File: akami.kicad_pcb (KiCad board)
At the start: 4 copper layers, 30 x 33.3 mm, 55 parts, among them J1 USB_C_Receptacle_USB2.0, Q1 P MOSFET, Q2 P MOSFET, U1 nRF52840, U2 TP4054, U3 AP2112K-3.3, U4 ProMicro_2, Y1 32MHz, Y2 32.768 kHz

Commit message: more stuff
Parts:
- added J2: Conn_01x01, footprints:1pin_conn, F.Cu at (7.62, -15.2)
- added J3: Conn_01x01, footprints:1pin_conn, F.Cu at (-7.62, -15.2)
- added TP3: TestPoint, TestPoint:TestPoint_Pad_1.0x1.0mm, B.Cu at (0.00, -5.85)
- added TP4: TestPoint, footprints:circular-pad-0.3mm, F.Cu at (-5.15, 12.8)
- C17, C18: value 12pF -> 3.3pF
- C6, C7: value 12pF -> 10pF
- mouse-bite-2mm-slot (x2): footprint panelisation:mouse-bite-2mm-slot -> footprints:mouse-bite-2mm-slot-one-sided
- moved R2 7.52 mm to (-0.95, -1.62), turned to 0 degrees
- moved C13 2.00 mm to (-4.30, 0.55), turned to 270 degrees
- moved C2 0.28 mm to (-2.03, 0.55)
- moved R4 0.09 mm to (-0.65, -0.01)
- moved R7 0.05 mm to (3.70, -2.44)
- turned mouse-bite-2mm-slot to 270 degrees
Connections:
- net Net-(C22-Pad2) renamed ANTENNA
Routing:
- net USB_D-: track 23.3 -> 21.2 mm
- net VBUS: track 37.1 -> 35.2 mm, vias 5 -> 6
- net P0.08: track 19.6 -> 17.8 mm
- net POWER_CTRL: track 21.3 -> 23.1 mm
- net P0.06: track 21.0 -> 19.3 mm
- net VBAT: track 33.5 -> 35.1 mm, vias 4 -> 6
- net RESET: track 20.6 -> 19.4 mm
- net P0.11: track 15.3 -> 14.1 mm
- net Net-(C13-Pad1): track 3.64 -> 4.70 mm
- net VDD_NRF: track 11.7 -> 12.7 mm, vias 8 -> 9
- net Net-(L3-Pad2): track 10.5 -> 9.63 mm
- net GND: track 36.1 -> 35.3 mm, vias 31 -> 38
- net BAT_VOLT: track 12.4 -> 11.6 mm
- net Net-(C15-Pad2): track 22.0 -> 21.5 mm
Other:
- board text added: "VDD"

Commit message: stuff
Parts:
- added G***: LOGO, footprints:akami-logo, F.Cu at (0.00, 13.5)
- added G***: LOGO, footprints:akami-logo, B.Cu at (0.00, 14.5)
- added NT1: Net-Tie_2, footprints:net-tie-2-tiny, F.Cu at (1.50, 7.33)
- C12: value 820pF -> 1nF
- C17, C18: value 3.3pF -> 15pF
- Q1, Q2: value P MOSFET -> AO3401A
- Y2: footprint Crystal:Crystal_SMD_2012-2Pin_2.0x1.2mm -> Crystal:Crystal_SMD_3215-2Pin_3.2x1.5mm
- moved C8 10.5 mm to (-2.45, 0.56), turned to 270 degrees
- moved C20 10.3 mm to (-6.00, -8.05), turned to 270 degrees
- moved C14 7.11 mm to (1.10, -1.90), turned to 180 degrees
- moved R2 4.58 mm to (-4.90, 0.70)
- moved C13 2.63 mm to (-2.17, -1.00), turned to 0 degrees
- moved R4 1.51 mm to (0.75, 0.54)
- moved C1 1.46 mm to (-2.42, 9.62)
- moved C22 1.20 mm to (3.90, 9.22), turned to 270 degrees
- moved C18 1.12 mm to (5.25, -2.65)
- moved C21 0.94 mm to (-4.90, -1.00), turned to 180 degrees
- moved C19 0.91 mm to (1.10, -0.80), turned to 180 degrees
- moved C2 0.66 mm to (-1.38, 0.56), turned to 270 degrees
- moved Y2 0.48 mm to (5.25, -0.35), turned to 270 degrees
- moved L3 0.38 mm to (-5.72, 5.08)
- moved C17 0.32 mm to (5.25, 1.95)
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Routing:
- net GND: track 35.3 -> 43.0 mm, vias 38 -> 53
- net POWER_CTRL: track 23.1 -> 19.0 mm, vias 3 -> 2
- net VDD_NRF: track 12.7 -> 16.6 mm, vias 9 -> 10
- net Net-(R11-Pad2): track 9.10 -> 5.49 mm, vias 2 -> 0
- net P0.10: track 10.4 -> 12.7 mm
- net P0.08: track 17.8 -> 20.1 mm
- net P0.09: track 12.5 -> 14.8 mm
- net Net-(C20-Pad2): track 15.2 -> 12.9 mm, vias 3 -> 2
- net RESET: track 19.4 -> 17.7 mm
- net P0.06: track 19.3 -> 20.7 mm, vias 3 -> 1
- net ANTENNA: track 36.8 -> 35.4 mm
- net BAT_VOLT: track 11.6 -> 10.3 mm
- net BLUE_LED: track 12.0 -> 13.2 mm
- net Net-(C17-Pad2): track 6.37 -> 7.48 mm
- net Net-(C15-Pad2): track 21.5 -> 22.6 mm
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- added copper zone on B.Cu, net GND
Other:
- board text added: "+"
- board text added: "JLCJLCJLCJLC"
- board text added: "Using a strip gap of 0.125 (copper fill clearance) and a distance to ground plane of 1.5mm (JLC 7628) [inner layers are removed] we get a track width of 0.6mm for 50 ohms."
- board text added: "rev 1"

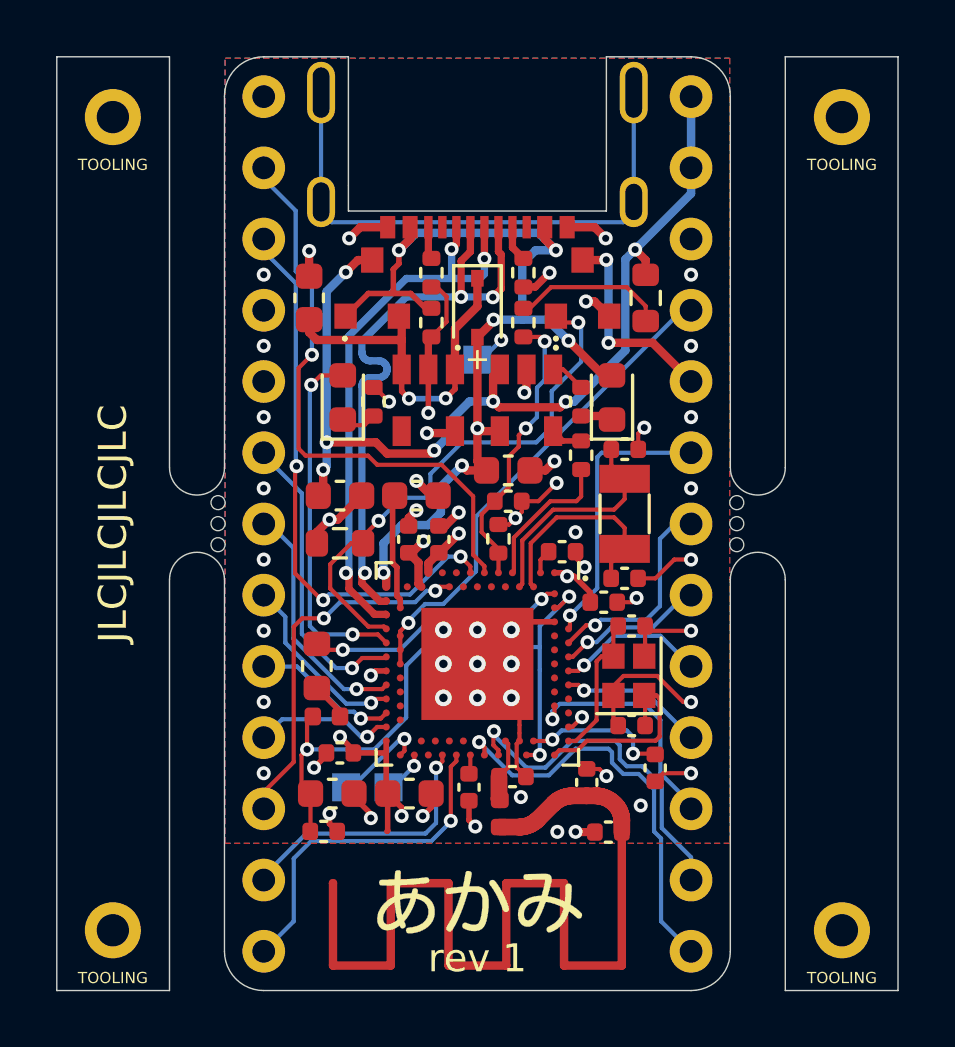
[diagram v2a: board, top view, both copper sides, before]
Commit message: add (experimental) rev 2, using VDDH (high voltage) input.
other things (related to switching to VDDH):
1. get rid of the power control mosfet; now uses the LDO (AP2112K)
   and its EN control to control EXT_VCC

2. related to (1), power output is now OFF by default -- drive the
   pin high to enable VCC out.

3. add a schottky diode (D4) to protect the LDO from reverse flow,
   while also letting current from EXT_VCC (eg. TRRS) drive the MCU
   and also any peripherals. (note that the driving side then can't
   disable peripheral [eg. OLED, EEPROM] power, for obvious reasons)

4. switch the schottky diode (D2) to a 1N5817 (from 819) to shrink
   the BOM, due to (3).

5. break out both VDDH and VDD_NRF on the back pads; silk markings
   are 'H' and 'L' respectively

6. layer 3 (inner layer 2) is now used to route some power traces
   (EXT_VCC, some VDD_HV). this reduces power dissipation a little

7. add a 1uF cap on EXT_VCC to stabilise the incoming power before
   it goes to VDDH
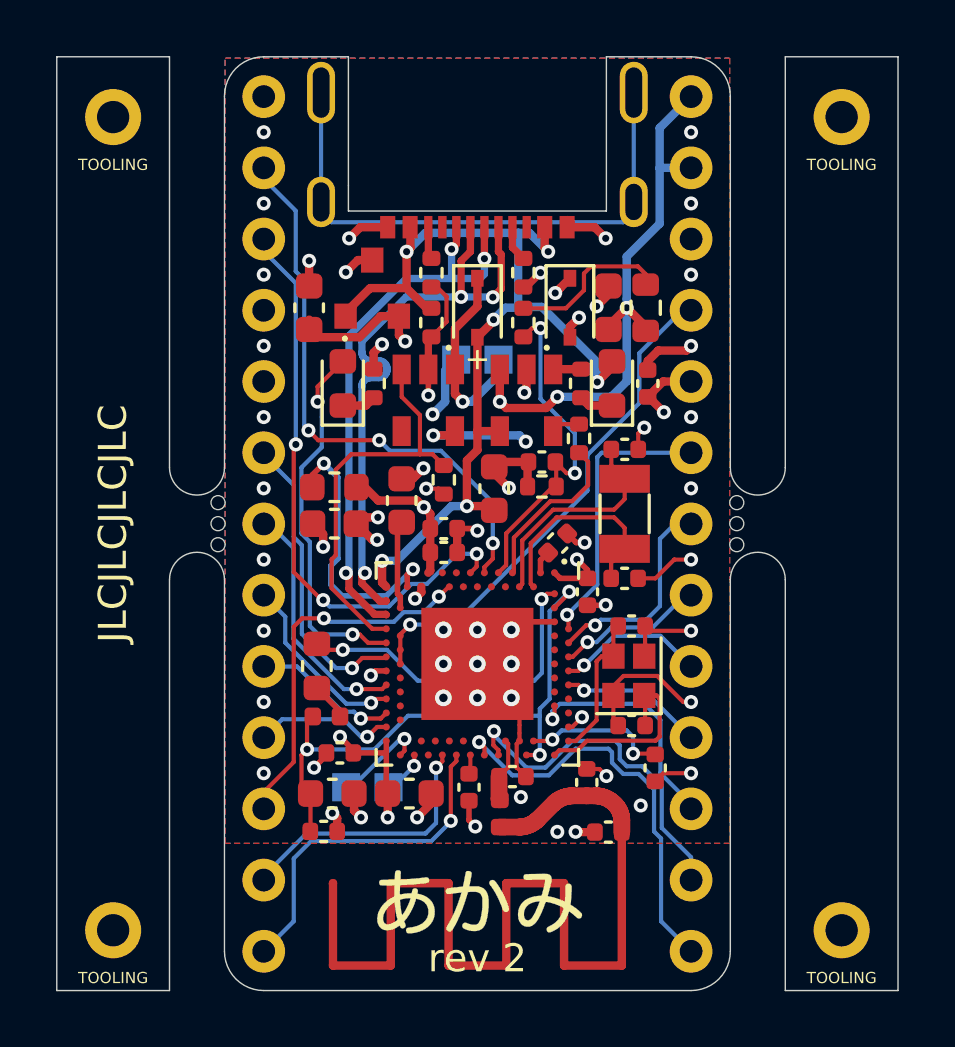
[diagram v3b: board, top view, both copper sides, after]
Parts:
- removed Q1: AO3401A, Package_TO_SOT_SMD:SOT-23
- removed R2: 2M, Resistor_SMD:R_0603_1608Metric
- removed REF** (x4): jlcpcb_tooling_hole, footprints:jlcpcb_tooling_hole
- added C23: 4.7uF, Capacitor_SMD:C_0603_1608Metric, F.Cu at (-5.10, 0.00)
- added C24: 1uF, Capacitor_SMD:C_0402_1005Metric, F.Cu at (6.08, -5.00)
- added D4: 1N5817, Diode_SMD:D_SOD-323, F.Cu at (3.30, -7.70)
- added DUMMY5: tooling_hole, footprints:jlcpcb_tooling_hole, F.Cu at (-13.0, -14.5)
- added DUMMY6: tooling_hole, footprints:jlcpcb_tooling_hole, F.Cu at (-13.0, 14.5)
- added DUMMY7: tooling_hole, footprints:jlcpcb_tooling_hole, F.Cu at (13.0, -14.5)
- added DUMMY8: tooling_hole, footprints:jlcpcb_tooling_hole, F.Cu at (13.0, 14.5)
- added L4: 10uH, Inductor_SMD:L_0603_1608Metric, F.Cu at (-5.10, -1.30)
- added R1: 1M, Resistor_SMD:R_0402_1005Metric, F.Cu at (-1.20, -1.56)
- added TP5: TestPoint, TestPoint:TestPoint_Pad_1.0x1.0mm, B.Cu at (0.76, -5.85)
- D2: value 1N5819 -> 1N5817
- DUMMY1: renamed from G***; value LOGO -> logo_front
- DUMMY2: renamed from G***; value LOGO -> logo_back
- DUMMY3: renamed from mouse-bite-2mm-slot; value VAL** -> mousebite_left
- DUMMY4: renamed from mouse-bite-2mm-slot; value VAL** -> mousebite_right
- moved C21 11.7 mm to (4.67, -7.70), turned to 270 degrees
- moved R4 2.43 mm to (2.30, -1.32), turned to 180 degrees
- moved C19 1.84 mm to (2.30, -2.20), turned to 0 degrees
- moved C8 1.31 mm to (-1.20, 0.17), turned to 0 degrees
- moved C14 0.82 mm to (0.60, -1.25), turned to 270 degrees
- moved TP3 0.76 mm to (-0.76, -5.85)
- moved C4 0.69 mm to (3.92, 2.43), turned to 270 degrees
- moved R5 0.65 mm to (-3.70, -5.00)
- moved R8 0.65 mm to (3.70, -5.00)
- moved R7 0.60 mm to (3.62, -3.04)
- moved C13 0.55 mm to (-2.70, -0.82), turned to 90 degrees
- moved D1 0.50 mm to (-4.80, -5.00)
- moved D3 0.50 mm to (4.80, -5.00)
- moved C2 0.50 mm to (-1.20, 1.02), turned to 180 degrees
- moved C20 0.35 mm to (-6.00, -7.70)
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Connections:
- C20 pad 2: Net-(C20-Pad2) -> VDD_HV
- C4 pad 1: GND -> VDD_NRF
- C4 pad 2: VDD_NRF -> GND
- C8 pad 1: GND -> VDD_NRF
- C8 pad 2: VDD_NRF -> GND
- D2 pad 1: Net-(C20-Pad2) -> VDD_HV
- Q2 pad 2: Net-(C20-Pad2) -> VDD_HV
- U1 pad Y2: VDD_NRF -> VDD_HV
- U3 pad 1: Net-(C20-Pad2) -> VDD_HV
- U3 pad 3: Net-(C20-Pad2) -> POWER_CTRL
- U3 pad 5: VDD_NRF -> EXT_VCC
- U4 pad 21: 3V3_OUT -> EXT_VCC
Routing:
- net VDD_HV: track 0.00 -> 35.7 mm, vias 0 -> 6
- net EXT_VCC: track 0.00 -> 16.4 mm, vias 0 -> 4
- net Net-(C20-Pad2): track 12.9 -> 0.00 mm, vias 2 -> 0
- net Net-(L4-Pad2): track 0.00 -> 9.85 mm, vias 0 -> 2
- net 3V3_OUT: track 7.36 -> 0.00 mm, vias 2 -> 0
- net VBAT: track 34.6 -> 29.1 mm, vias 7 -> 4
- net POWER_CTRL: track 19.0 -> 14.4 mm, vias 2 -> 0
- net Net-(L3-Pad2): track 9.39 -> 11.9 mm
- net BAT_VOLT: track 10.3 -> 12.2 mm
- net Net-(C15-Pad2): track 22.6 -> 20.7 mm
- net VDD_NRF: track 16.6 -> 15.5 mm, vias 10 -> 7
- net Net-(C13-Pad1): track 4.14 -> 3.15 mm
- net P0.08: track 20.1 -> 21.0 mm
- net CHARGE_CTRL: track 5.24 -> 5.99 mm
- net GND: track 43.0 -> 43.7 mm, vias 53 -> 55
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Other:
- board text added: "H"
- board text added: "L"
- board text added: "rev 2"
- board text removed: "VDD"
- board text removed: "rev 1"
